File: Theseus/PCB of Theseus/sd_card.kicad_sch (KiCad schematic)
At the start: 6 parts, among them J6 Micro_SD_Card

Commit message: Theseus_Dev_Rev2
It's still the same PCB
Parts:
- added C26: 10u, Capacitor_SMD:C_0805_2012Metric_Pad1.18x1.45mm_HandSolder, symbol Device:C
- J6: value Micro_SD_Card -> Micro SD Holder 0472192001
- R13, R14, R15, R16, R17: footprint Resistor_SMD:R_0402_1005Metric_Pad0.72x0.64mm_HandSolder -> Resistor_SMD:R_0805_2012Metric_Pad1.20x1.40mm_HandSolder; symbol Device:R_Small_US -> Device:R_US
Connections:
- net +3.3V: now also C26.1
- net GND: now also C26.2

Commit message: Flight design, first pass
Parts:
- R13, R14, R15, R16, R17: value 50k -> 51k
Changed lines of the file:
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@@
 			)
 		)
-		(property "Value" "50k"
+		(property "Value" "51k"
 			(at 73.66 81.2799 0)
 			(effects
@@
 			)
 		)
-		(property "Value" "50k"
+		(property "Value" "51k"
 			(at 85.09 81.2799 0)
 			(effects
@@
 			)
 		)
-		(property "Value" "50k"
+		(property "Value" "51k"
 			(at 107.95 81.2799 0)
 			(effects
@@
 			)
 		)
-		(property "Value" "50k"
+		(property "Value" "51k"
 			(at 60.96 81.2799 0)
 			(effects
@@
 			)
 		)
-		(property "Value" "50k"
+		(property "Value" "51k"
 			(at 95.25 81.2799 0)
 			(effects

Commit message: Flight design v1
First pass at flight design
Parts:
- C26: footprint Capacitor_SMD:C_0805_2012Metric_Pad1.18x1.45mm_HandSolder -> Capacitor_SMD:C_0603_1608Metric_Pad1.08x0.95mm_HandSolder
- R13, R14, R15, R16, R17: footprint Resistor_SMD:R_0805_2012Metric_Pad1.20x1.40mm_HandSolder -> Resistor_SMD:R_0603_1608Metric_Pad0.98x0.95mm_HandSolder
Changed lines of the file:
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@@
 			)
 		)
-		(property "Footprint" "Resistor_SMD:R_0805_2012Metric_Pad1.20x1.40mm_HandSolder"
+		(property "Footprint" "Resistor_SMD:R_0603_1608Metric_Pad0.98x0.95mm_HandSolder"
 			(at 72.136 80.264 90)
 			(effects
@@
 			)
 		)
-		(property "Footprint" "Resistor_SMD:R_0805_2012Metric_Pad1.20x1.40mm_HandSolder"
+		(property "Footprint" "Resistor_SMD:R_0603_1608Metric_Pad0.98x0.95mm_HandSolder"
 			(at 83.566 80.264 90)
 			(effects
@@
 			)
 		)
-		(property "Footprint" "Resistor_SMD:R_0805_2012Metric_Pad1.20x1.40mm_HandSolder"
+		(property "Footprint" "Resistor_SMD:R_0603_1608Metric_Pad0.98x0.95mm_HandSolder"
 			(at 106.426 80.264 90)
 			(effects
@@
 			)
 		)
-		(property "Footprint" "Resistor_SMD:R_0805_2012Metric_Pad1.20x1.40mm_HandSolder"
+		(property "Footprint" "Resistor_SMD:R_0603_1608Metric_Pad0.98x0.95mm_HandSolder"
 			(at 59.436 80.264 90)
 			(effects
@@
 			)
 		)
-		(property "Footprint" "Resistor_SMD:R_0805_2012Metric_Pad1.20x1.40mm_HandSolder"
+		(property "Footprint" "Resistor_SMD:R_0603_1608Metric_Pad0.98x0.95mm_HandSolder"
 			(at 93.726 80.264 90)
 			(effects
@@
 			)
 		)
-		(property "Footprint" "Capacitor_SMD:C_0805_2012Metric_Pad1.18x1.45mm_HandSolder"
+		(property "Footprint" "Capacitor_SMD:C_0603_1608Metric_Pad1.08x0.95mm_HandSolder"
 			(at 225.7552 101.6 0)
 			(effects

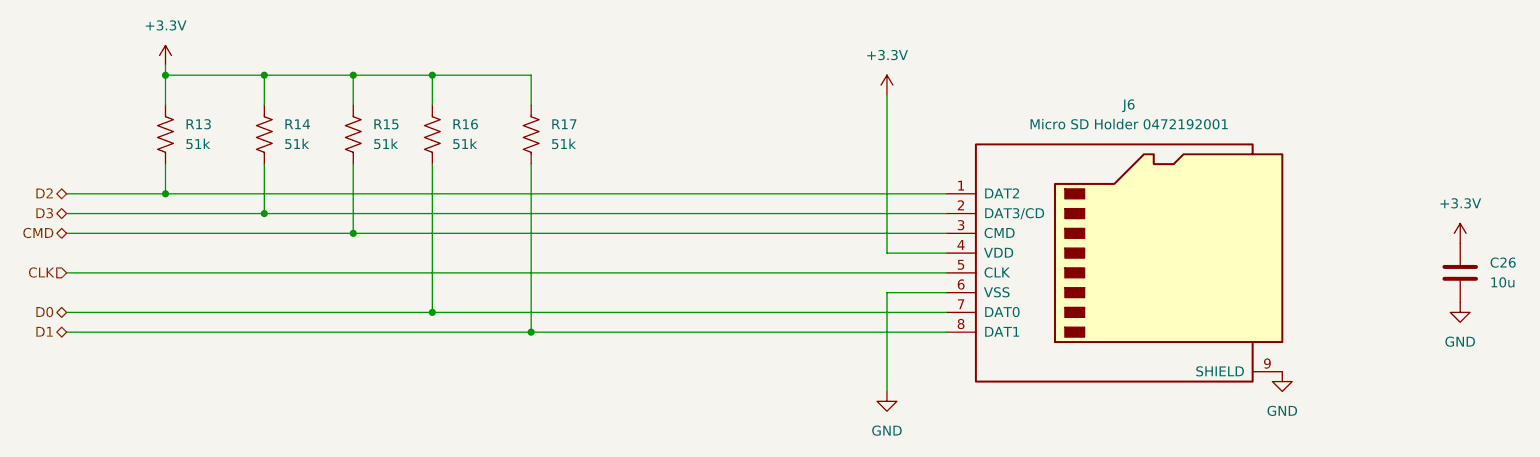
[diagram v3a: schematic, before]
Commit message: layout and routing + minor schematic changes
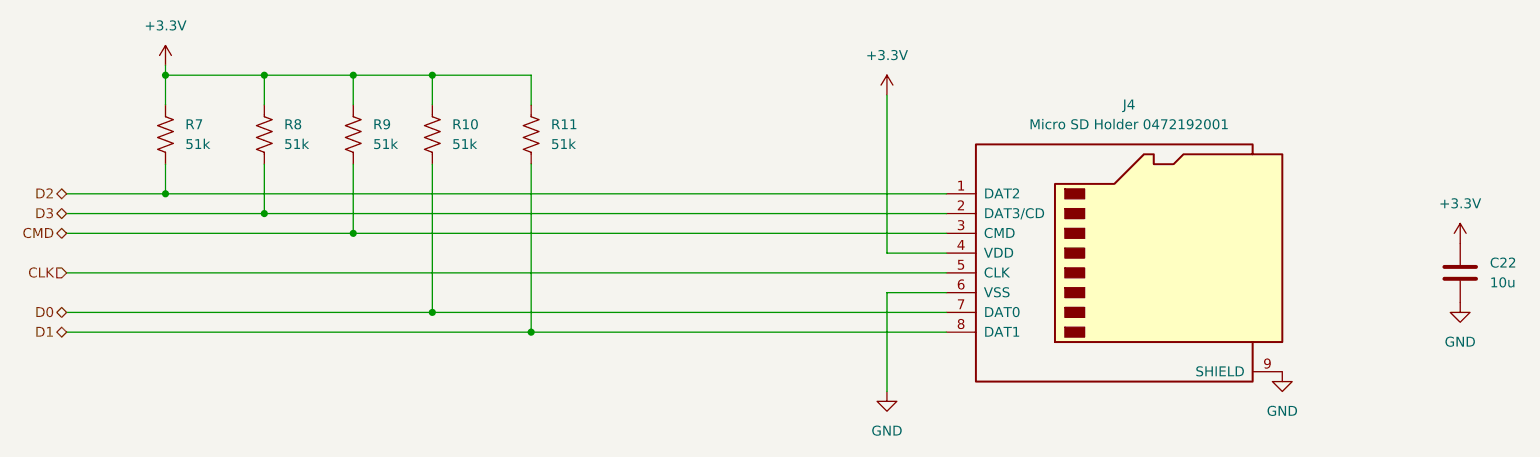
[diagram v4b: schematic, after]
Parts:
- renumbered C26 to C22, J6 to J4, R16 to R10, R17 to R11, R13 to R7, R14 to R8, R15 to R9
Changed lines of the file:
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@@
 		(dnp no)
 		(fields_autoplaced yes)
-		(property "Reference" "J6"
+		(property "Reference" "J4"
 			(at 182.245 76.2 0)
 			(effects
@@
 			(project ""
 				(path "/4bacb39c-4494-4a9f-9fe3-1fedf5cd381a/69868668-3056-4d52-8e9d-cd07748d784f"
-					(reference "J6")
+					(reference "J4")
 					(unit 1)
 				)
@@
 		(dnp no)
 		(fields_autoplaced yes)
-		(property "Reference" "#PWR031"
+		(property "Reference" "#PWR036"
 			(at 151.13 119.38 0)
 			(effects
@@
 			(project ""
 				(path "/4bacb39c-4494-4a9f-9fe3-1fedf5cd381a/69868668-3056-4d52-8e9d-cd07748d784f"
-					(reference "#PWR031")
+					(reference "#PWR036")
 					(unit 1)
 				)
@@
 		(dnp no)
 		(fields_autoplaced yes)
-		(property "Reference" "R14"
+		(property "Reference" "R8"
 			(at 73.66 78.7399 0)
 			(effects
@@
 			(project ""
 				(path "/4bacb39c-4494-4a9f-9fe3-1fedf5cd381a/69868668-3056-4d52-8e9d-cd07748d784f"
-					(reference "R14")
+					(reference "R8")
 					(unit 1)
 				)
@@
 		(dnp no)
 		(fields_autoplaced yes)
-		(property "Reference" "R15"
+		(property "Reference" "R9"
 			(at 85.09 78.7399 0)
 			(effects
@@
 			(project ""
 				(path "/4bacb39c-4494-4a9f-9fe3-1fedf5cd381a/69868668-3056-4d52-8e9d-cd07748d784f"
-					(reference "R15")
+					(reference "R9")
 					(unit 1)
 				)
@@
 		(on_board yes)
 		(dnp no)
-		(property "Reference" "R17"
+		(property "Reference" "R11"
 			(at 107.95 78.7399 0)
 			(effects
@@
 			(project ""
 				(path "/4bacb39c-4494-4a9f-9fe3-1fedf5cd381a/69868668-3056-4d52-8e9d-cd07748d784f"
-					(reference "R17")
+					(reference "R11")
 					(unit 1)
 				)
@@
 		(dnp no)
 		(fields_autoplaced yes)
-		(property "Reference" "R13"
+		(property "Reference" "R7"
 			(at 60.96 78.7399 0)
 			(effects
@@
 			(project ""
 				(path "/4bacb39c-4494-4a9f-9fe3-1fedf5cd381a/69868668-3056-4d52-8e9d-cd07748d784f"
-					(reference "R13")
+					(reference "R7")
 					(unit 1)
 				)
@@
 		(dnp no)
 		(fields_autoplaced yes)
-		(property "Reference" "#PWR022"
+		(property "Reference" "#PWR034"
 			(at 58.42 74.93 0)
 			(effects
@@
 			(project ""
 				(path "/4bacb39c-4494-4a9f-9fe3-1fedf5cd381a/69868668-3056-4d52-8e9d-cd07748d784f"
-					(reference "#PWR022")
+					(reference "#PWR034")
 					(unit 1)
 				)
@@
 		(dnp no)
 		(fields_autoplaced yes)
-		(property "Reference" "#PWR047"
+		(property "Reference" "#PWR039"
 			(at 224.79 107.95 0)
 			(effects
@@
 			(project "PCB of Theseus"
 				(path "/4bacb39c-4494-4a9f-9fe3-1fedf5cd381a/69868668-3056-4d52-8e9d-cd07748d784f"
-					(reference "#PWR047")
+					(reference "#PWR039")
 					(unit 1)
 				)
@@
 		(dnp no)
 		(fields_autoplaced yes)
-		(property "Reference" "#PWR030"
+		(property "Reference" "#PWR037"
 			(at 201.93 116.84 0)
 			(effects
@@
 			(project ""
 				(path "/4bacb39c-4494-4a9f-9fe3-1fedf5cd381a/69868668-3056-4d52-8e9d-cd07748d784f"
-					(reference "#PWR030")
+					(reference "#PWR037")
 					(unit 1)
 				)
@@
 		(dnp no)
 		(fields_autoplaced yes)
-		(property "Reference" "R16"
+		(property "Reference" "R10"
 			(at 95.25 78.7399 0)
 			(effects
@@
 			(project ""
 				(path "/4bacb39c-4494-4a9f-9fe3-1fedf5cd381a/69868668-3056-4d52-8e9d-cd07748d784f"
-					(reference "R16")
+					(reference "R10")
 					(unit 1)
 				)
@@
 		(dnp no)
 		(fields_autoplaced yes)
-		(property "Reference" "#PWR046"
+		(property "Reference" "#PWR038"
 			(at 224.79 97.79 0)
 			(effects
@@
 			(project "PCB of Theseus"
 				(path "/4bacb39c-4494-4a9f-9fe3-1fedf5cd381a/69868668-3056-4d52-8e9d-cd07748d784f"
-					(reference "#PWR046")
+					(reference "#PWR038")
 					(unit 1)
 				)
@@
 		(dnp no)
 		(fields_autoplaced yes)
-		(property "Reference" "C26"
+		(property "Reference" "C22"
 			(at 228.6 96.5199 0)
 			(effects
@@
 			(project ""
 				(path "/4bacb39c-4494-4a9f-9fe3-1fedf5cd381a/69868668-3056-4d52-8e9d-cd07748d784f"
-					(reference "C26")
+					(reference "C22")
 					(unit 1)
 				)
@@
 		(dnp no)
 		(fields_autoplaced yes)
-		(property "Reference" "#PWR032"
+		(property "Reference" "#PWR035"
 			(at 151.13 78.74 0)
 			(effects
@@
 			(project ""
 				(path "/4bacb39c-4494-4a9f-9fe3-1fedf5cd381a/69868668-3056-4d52-8e9d-cd07748d784f"
-					(reference "#PWR032")
-					(unit 1)
-				)
+					(reference "#PWR035")
+					(unit 1)
+				)
